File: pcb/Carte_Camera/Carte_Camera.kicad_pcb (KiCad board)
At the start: 2 copper layers, 22 x 23 mm, 5 parts, among them J1 Samtec FTS-105-01-L-DV, U1 TSL1401CL

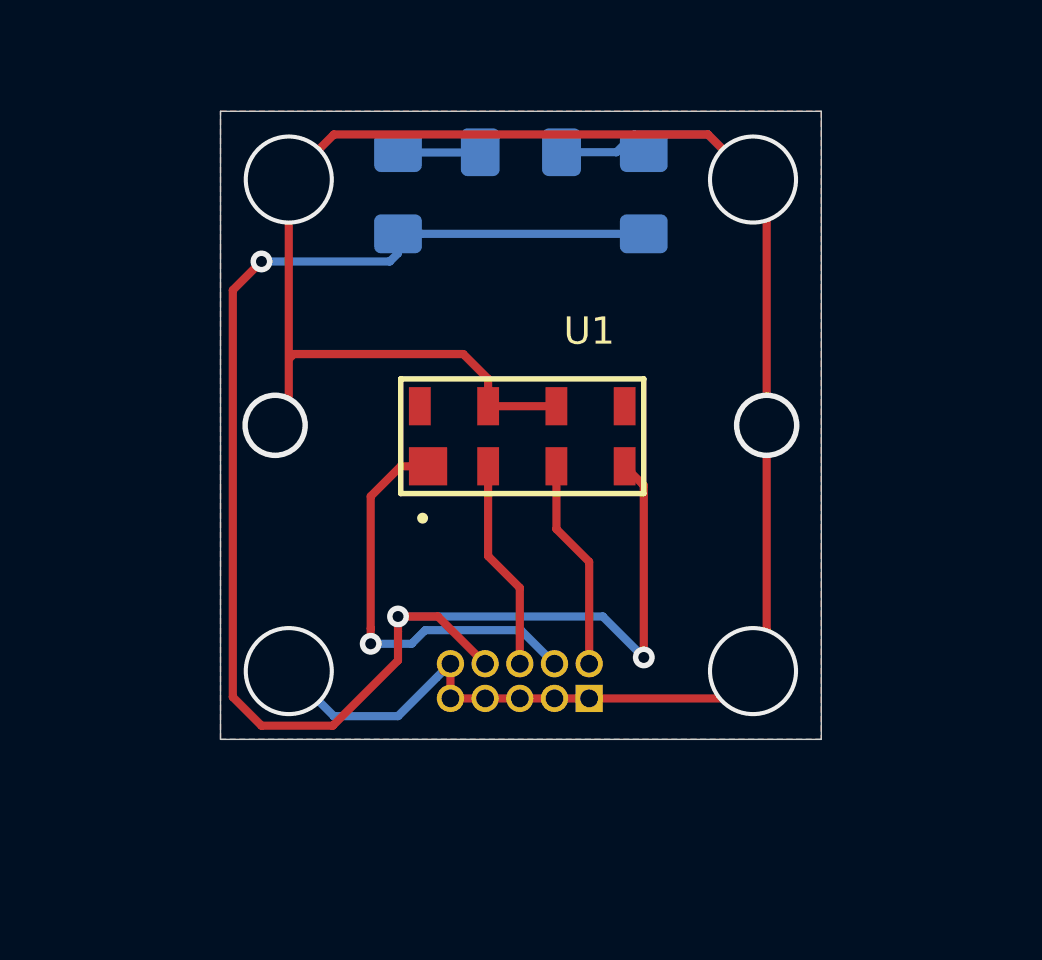
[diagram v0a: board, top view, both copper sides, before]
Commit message: ajout de la carte chassi DFRobotics + creation d'une nouvelle carte led + creation d'une carte capteur pour DFRobotic + correction de l'alimentation en 5V des encodeurs sur DFRobotic (carte Landzo a corriger dans un prochaine commit)
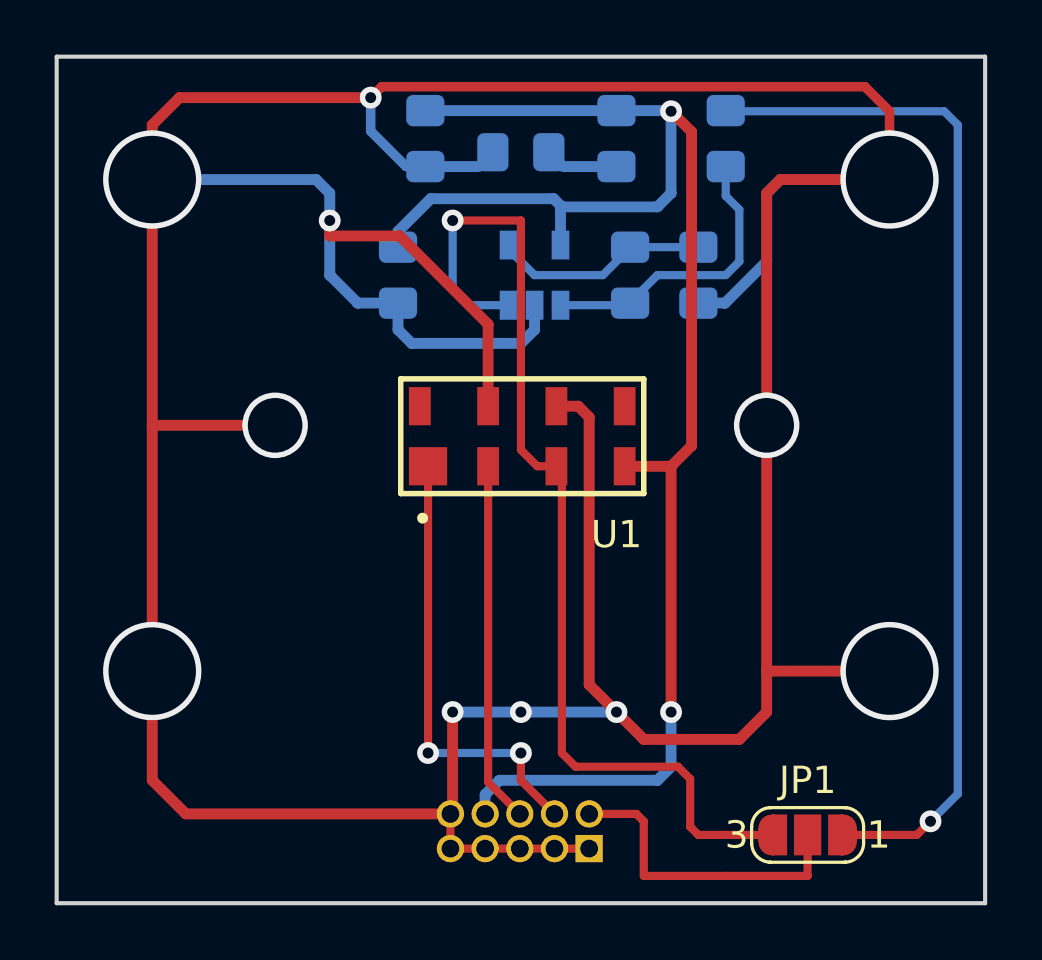
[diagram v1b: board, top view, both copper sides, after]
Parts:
- added C2: 1µF, Capacitor_SMD:C_0805_2012Metric_Pad1.15x1.40mm_HandSolder, B.Cu at (126.5, 103.0)
- added JP1: SolderJumper_3_Open, Jumper:SolderJumper-3_P1.3mm_Open_RoundedPad1.0x1.5mm_NumberLabels, F.Cu at (141.5, 123.5)
- added R2: 1K, Resistor_SMD:R_0805_2012Metric_Pad1.15x1.40mm_HandSolder, B.Cu at (135.0, 103.0)
- added R3: 1K, Resistor_SMD:R_0805_2012Metric_Pad1.15x1.40mm_HandSolder, B.Cu at (137.5, 103.0)
- added R4: 0, Resistor_SMD:R_0805_2012Metric_Pad1.15x1.40mm_HandSolder, B.Cu at (138.5, 98.0)
- added U2: TSV911AILT, Package_TO_SOT_SMD:SOT-23-5, B.Cu at (131.5, 103.0)
- C1: footprint Capacitor_SMD:C_1206_3216Metric_Pad1.42x1.75mm_HandSolder -> Capacitor_SMD:C_0805_2012Metric_Pad1.15x1.40mm_HandSolder
- D1: footprint LED_SMD:LED_1206_3216Metric_Pad1.42x1.75mm_HandSolder -> LED_SMD:LED_0805_2012Metric_Pad1.15x1.40mm_HandSolder
- R1: value R -> 680R; footprint Resistor_SMD:R_1206_3216Metric_Pad1.42x1.75mm_HandSolder -> Resistor_SMD:R_0805_2012Metric_Pad1.15x1.40mm_HandSolder
- moved C1 8.25 mm to (127.5, 98.0), turned to 270 degrees
- moved R1 8.25 mm to (134.5, 98.0), turned to 270 degrees
- moved J1 5.50 mm to (133.5, 124.0)
- turned D1 to 0 degrees
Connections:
- U1 pad 3: /CCD_AO -> Net-(JP1-Pad3)
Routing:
- net GND: track 86.4 -> 182.1 mm, vias 6 -> 11
- net Net-(JP1-Pad3): track 0.00 -> 37.8 mm, vias 0 -> 1
- net Net-(JP1-Pad1): track 0.00 -> 37.6 mm, vias 0 -> 1
- net Net-(R2-Pad2): track 0.00 -> 10.9 mm
- net Net-(R2-Pad1): track 0.00 -> 7.93 mm
- net /CCD_CLK: track 7.71 -> 13.2 mm
- net /CCD_AO: track 7.73 -> 11.6 mm
- net +3V3: track 61.1 -> 59.1 mm, vias 3 -> 2
- net /CCD_SI: track 15.4 -> 16.6 mm, vias 1 -> 2
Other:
- board size 22 x 23 mm -> 34 x 31 mm
